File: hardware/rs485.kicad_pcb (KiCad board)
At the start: 2 copper layers, 40 x 40 mm, 43 parts, among them P1 CON-SENSOR, P2 BOOT, P3 CONN_5, SW1 SW_DIP_4, U1 XMC1XXX48, U2 DRILL, U3 DRILL, U4 DRILL, U5 DRILL, U6 SP3491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

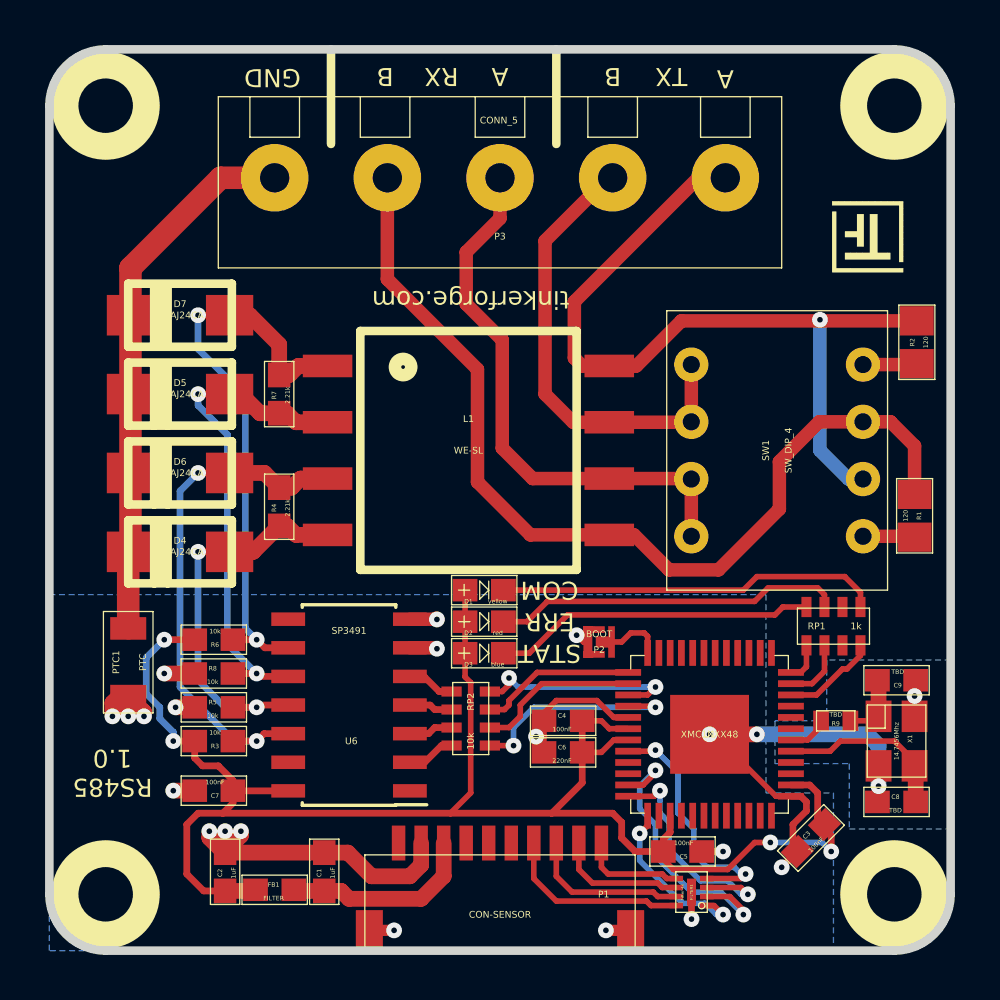
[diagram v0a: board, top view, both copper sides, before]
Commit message: add wee, ce logos, dip description, fiducials
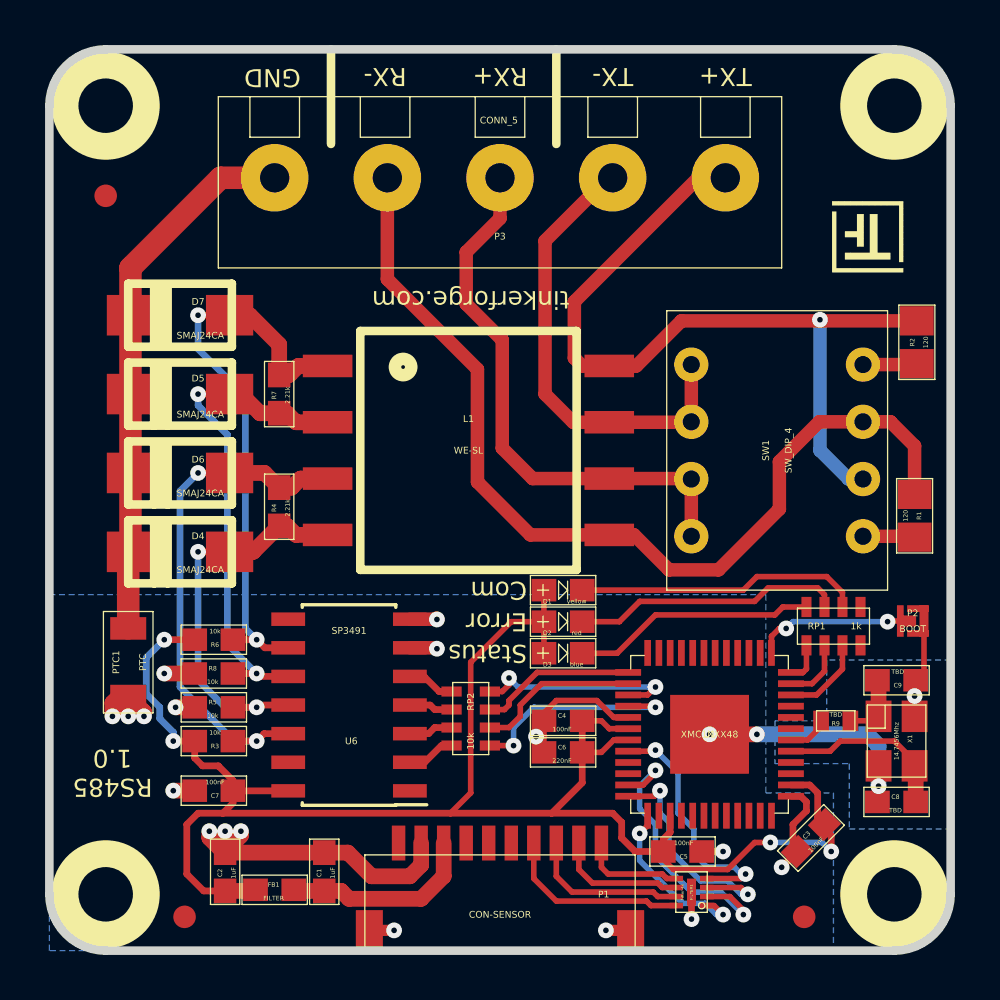
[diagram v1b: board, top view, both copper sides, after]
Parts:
- added Fiducial_Mark: VAL**, kicad-libraries:Fiducial_Mark, F.Cu at (158.8, 121.6)
- added Fiducial_Mark: VAL**, kicad-libraries:Fiducial_Mark, F.Cu at (127.8, 89.6)
- added Fiducial_Mark: VAL**, kicad-libraries:Fiducial_Mark, F.Cu at (131.3, 121.6)
- added VAL: WEEE_7mm_back, kicad-libraries:WEEE_7mm_back, B.Cu at (157.6, 100.1)
- added VAL: CE_5mm, kicad-libraries:CE_5mm, B.Cu at (157.3, 108.1)
- moved P2 13.9 mm to (163.6, 108.5), turned to 180 degrees
- moved D1 3.50 mm to (148.1, 107.1)
- moved D2 3.50 mm to (148.1, 108.5)
- moved D3 3.50 mm to (148.1, 109.9)
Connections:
- RP1 pad 1: Net-(D1-Pad2) -> (no net)
- RP1 pad 2: (no net) -> Net-(D1-Pad2)
- RP1 pad 7: (no net) -> Net-(RP1-Pad7)
- RP1 pad 8: Net-(RP1-Pad8) -> (no net)
- U1 pad 1: (no net) -> Net-(P2-Pad2)
- U1 pad 12: Net-(P2-Pad2) -> (no net)
- U1 pad 46: Net-(RP1-Pad8) -> Net-(RP1-Pad7)
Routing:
- net Net-(D1-Pad2): track 17.0 -> 12.2 mm
- net Net-(RP1-Pad8): track 4.26 -> 0.00 mm
- net Net-(P2-Pad2): track 2.97 -> 7.14 mm, vias 0 -> 2
- net Net-(D2-Pad2): track 15.5 -> 11.5 mm
- net Net-(D3-Pad2): track 14.3 -> 10.3 mm
- net Net-(RP1-Pad7): track 0.00 -> 3.81 mm
- net VCC: track 76.2 -> 79.4 mm
- net GND: track 57.6 -> 55.2 mm, vias 22 -> 21
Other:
- board text added: "1"
- board text added: "2"
- board text added: "3"
- board text added: "4"
- board text added: "Com"
- board text added: "Error"
- board text added: "Full Duplex Non Terminated"
- board text added: "Full Duplex Terminated"
- board text added: "Half Duplex Non Terminated"
- board text added: "Half Duplex Terminated"
- board text added: "ON"
- board text added: "RX+"
- board text added: "RX-"
- board text added: "Status"
- board text added: "TX+"
- board text added: "TX-"
- board text removed: "A"
- board text removed: "B"
- board text removed: "COM"
- board text removed: "ERR"
- board text removed: "RX"
- board text removed: "STAT"
- board text removed: "TX"

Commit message: ordered first prototype
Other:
- board text added: "Full-Duplex Non-Terminated"
- board text added: "Full-Duplex Terminated"
- board text added: "Half-Duplex Non-Terminated"
- board text added: "Half-Duplex Terminated"
- board text removed: "Full Duplex Non Terminated"
- board text removed: "Full Duplex Terminated"
- board text removed: "Half Duplex Non Terminated"
- board text removed: "Half Duplex Terminated"
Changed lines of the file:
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@@
     (visible_elements FFFF7FBF)
     (pcbplotparams
-      (layerselection 0x00030_80000001)
+      (layerselection 0x010f8_80000001)
       (usegerberextensions true)
       (excludeedgelayer true)
@@
     (effects (font (size 0.8 0.8) (thickness 0.15)) (justify mirror))
   )
-  (gr_text "Full Duplex\nTerminated" (at 137.5 112.1 270) (layer B.SilkS)
+  (gr_text "Full-Duplex\nTerminated" (at 137.5 112.1 270) (layer B.SilkS)
     (effects (font (size 0.8 0.8) (thickness 0.15)) (justify mirror))
   )
-  (gr_text "Full Duplex\nNon Terminated" (at 149.55 112.1 270) (layer B.SilkS)
+  (gr_text "Full-Duplex\nNon-Terminated" (at 149.55 112.1 270) (layer B.SilkS)
     (effects (font (size 0.8 0.8) (thickness 0.15)) (justify mirror))
   )
@@
     (effects (font (size 0.8 0.8) (thickness 0.15)) (justify mirror))
   )
-  (gr_text "Half Duplex\nNon Terminated" (at 149.55 100.7 270) (layer B.SilkS)
+  (gr_text "Half-Duplex\nNon-Terminated" (at 149.55 100.7 270) (layer B.SilkS)
     (effects (font (size 0.8 0.8) (thickness 0.15)) (justify mirror))
   )
-  (gr_text "Half Duplex\nTerminated" (at 137.5 100.7 270) (layer B.SilkS)
+  (gr_text "Half-Duplex\nTerminated" (at 137.5 100.7 270) (layer B.SilkS)
     (effects (font (size 0.8 0.8) (thickness 0.15)) (justify mirror))
   )

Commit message: specify crystal and capacitors
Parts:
- C8, C9: value TBD -> 10pF
- X1: value 14.7456Mhz -> 16Mhz
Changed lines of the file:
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@@
     (links 107)
     (no_connects 0)
-    (area 125.109499 82.909499 165.490501 123.290501)
+    (area 124.445139 82.245139 282.895869 162.490743)
     (thickness 1.6002)
     (drawings 125)
@@
   )
   (setup
-    (last_trace_width 0.25)
+    (last_trace_width 0.249)
     (user_trace_width 0.25)
     (user_trace_width 0.29972)
@@
       (effects (font (size 0.2 0.2) (thickness 0.05)))
     )
-    (fp_text value TBD (at 0.05 -0.375 180) (layer F.SilkS)
+    (fp_text value 10pF (at 0.05 -0.375 180) (layer F.SilkS)
       (effects (font (size 0.2 0.2) (thickness 0.05)))
     )
@@
       (effects (font (size 0.2 0.2) (thickness 0.05)))
     )
-    (fp_text value TBD (at 0.05 -0.375) (layer F.SilkS)
+    (fp_text value 10pF (at 0.05 -0.375) (layer F.SilkS)
       (effects (font (size 0.2 0.2) (thickness 0.05)))
     )
@@
       (effects (font (size 0.2 0.2) (thickness 0.05)))
     )
-    (fp_text value 14.7456Mhz (at 0 0 270) (layer F.SilkS)
-      (effects (font (size 0.2 0.2) (thickness 0.05)))
-    )
+    (fp_text value 16Mhz (at 0 0 270) (layer F.SilkS)
+      (effects (font (size 0.2 0.2) (thickness 0.05)))
+    )

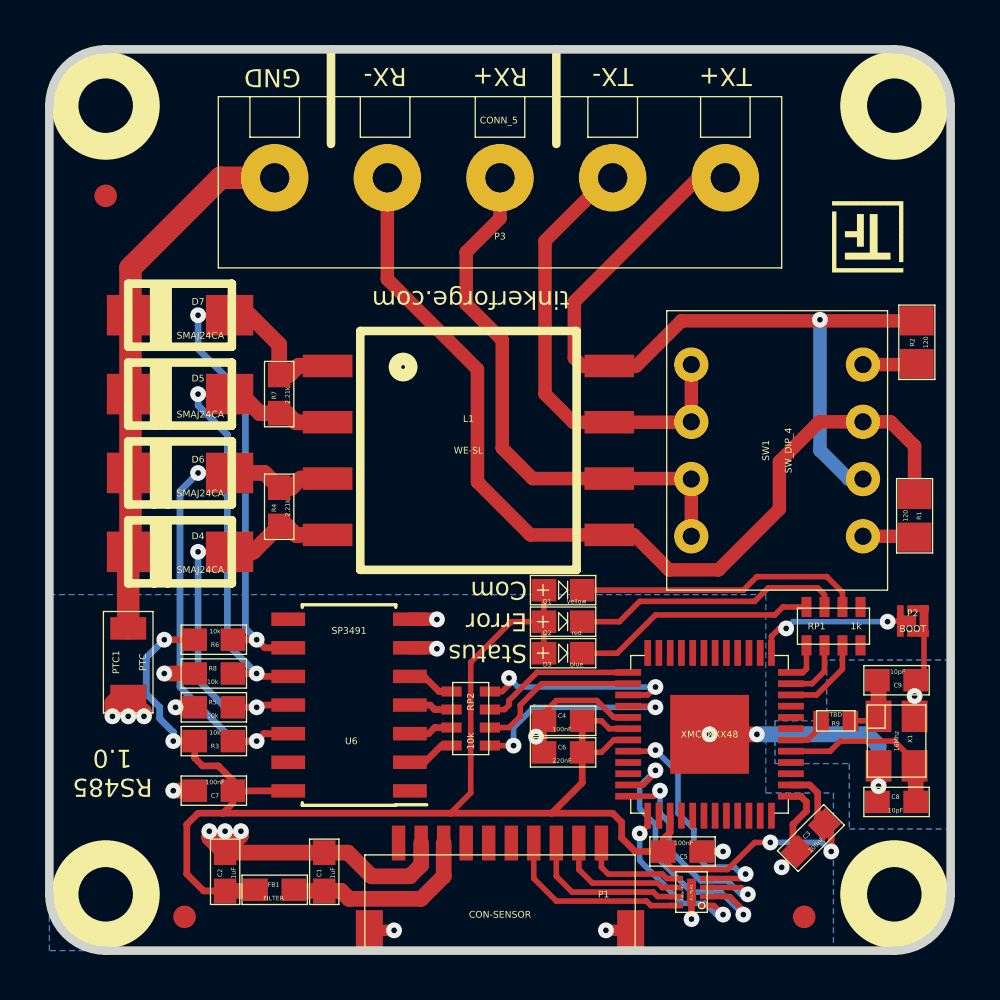
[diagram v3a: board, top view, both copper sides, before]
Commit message: fix footprints
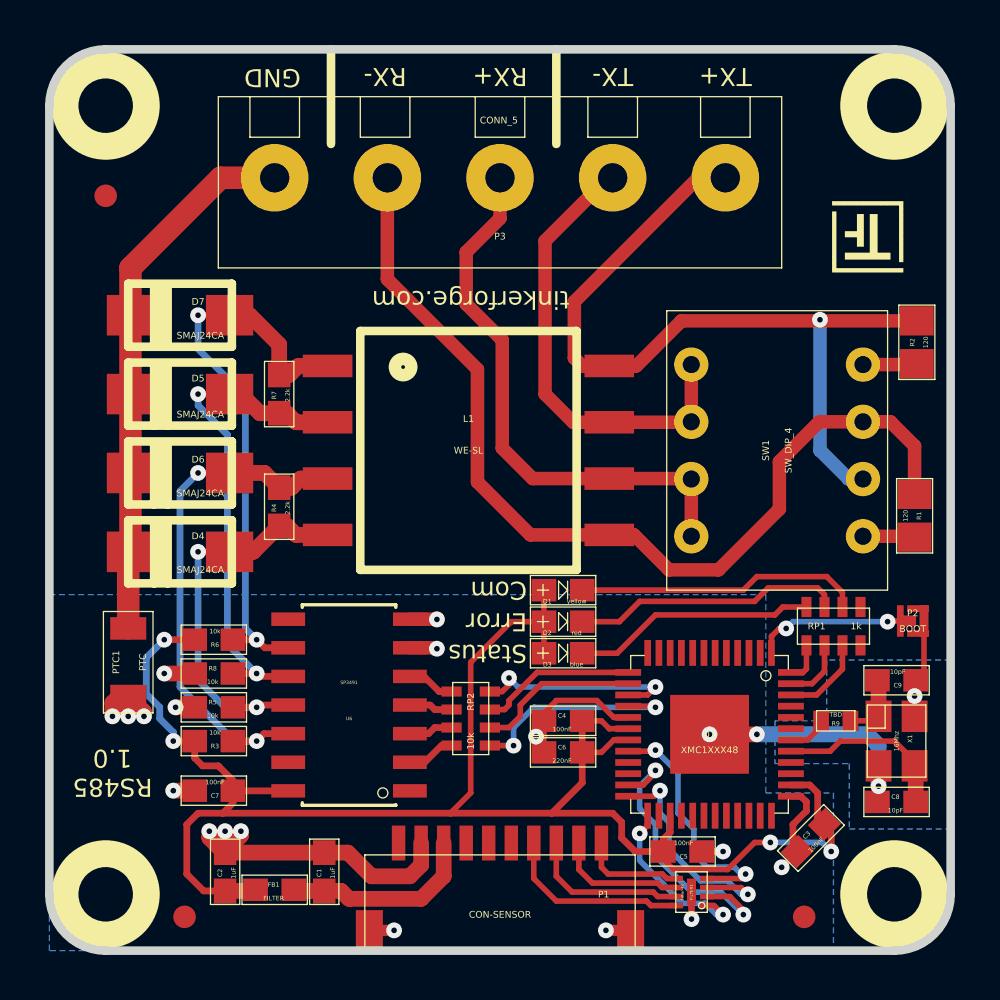
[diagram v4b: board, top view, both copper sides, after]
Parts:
- R4, R7: value 2.21k -> 2.2k
- U6: footprint SOIC-14_3.9x8.7mm_Pitch1.27mm -> kicad-libraries:SOIC-14_3.9x8.7mm_Pitch1.27mm

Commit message: add comcu icon
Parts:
- added G***: LOGO, kicad-libraries:Logo_CoMCU, B.Cu at (157.6, 115.3)
- moved VAL 0.30 mm to (157.6, 108.1)

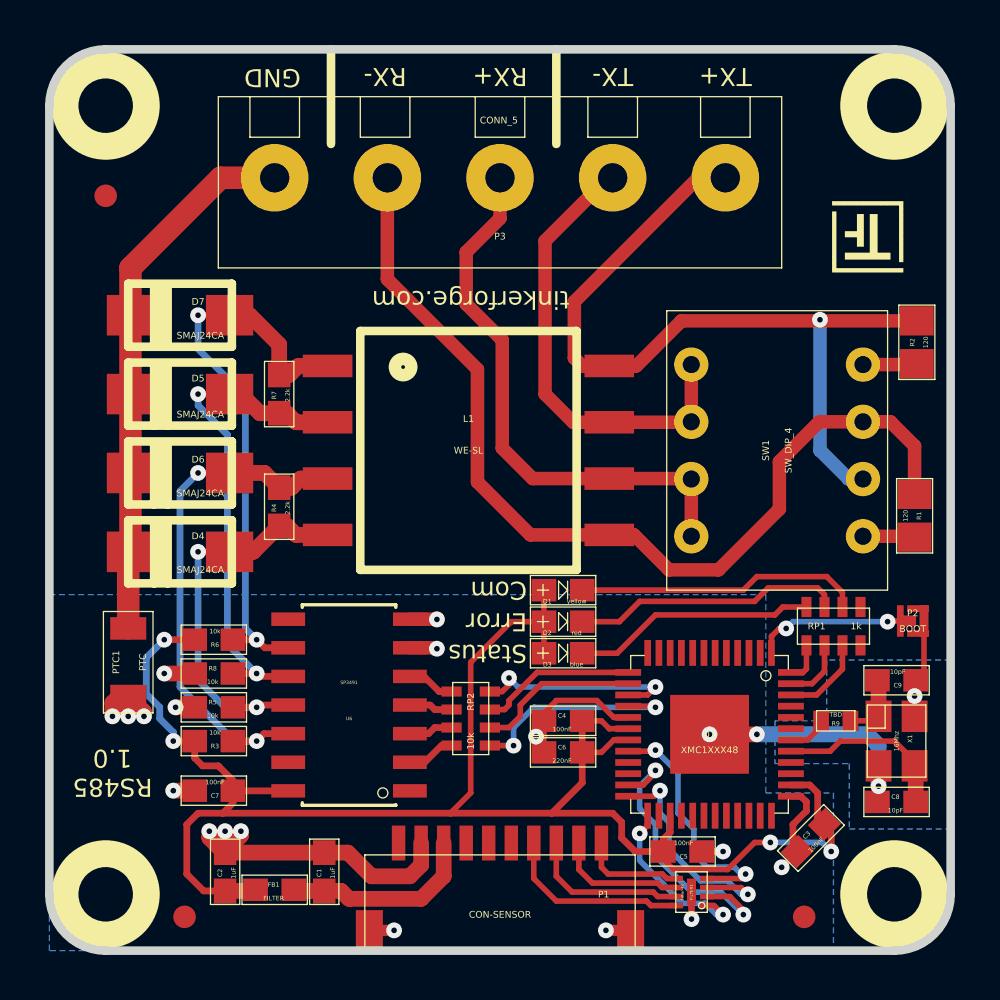
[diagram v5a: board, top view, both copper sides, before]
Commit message: change bricklet connector to 7pole JST GH connector
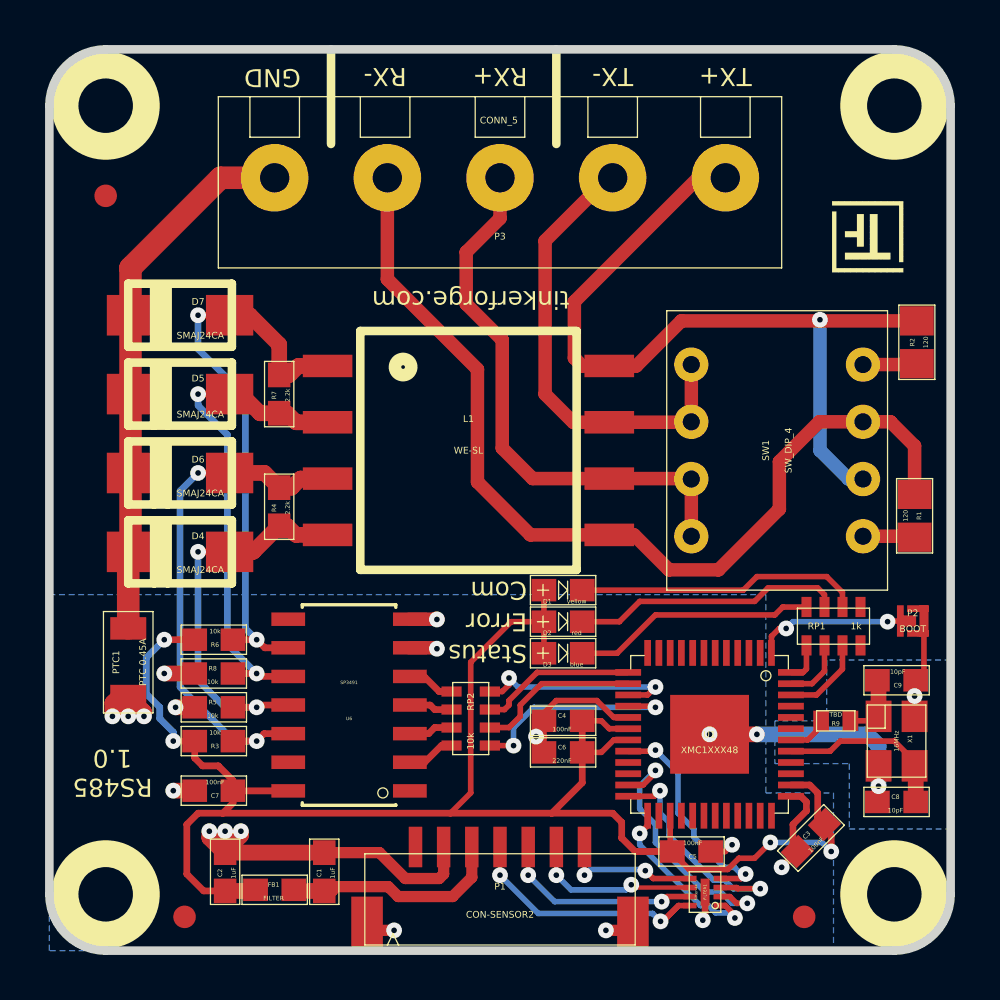
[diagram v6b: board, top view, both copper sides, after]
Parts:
- P1: value CON-SENSOR -> CON-SENSOR2; footprint CON-SENSOR -> kicad-libraries:CON-SENSOR2
- PTC1: value PTC -> PTC 0.45A
- X1: value 16Mhz -> 16MHz
- moved FILTER1 0.60 mm to (154.4, 120.5)
- moved C5 0.40 mm to (153.8, 118.7)
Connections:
- P1 pad 4: (no net) -> Net-(FILTER1-Pad8)
- P1 pad 5: (no net) -> Net-(FILTER1-Pad7)
- P1 pad 6: (no net) -> Net-(FILTER1-Pad6)
- P1 pad 7: Net-(FILTER1-Pad8) -> Net-(FILTER1-Pad5)
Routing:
- net Net-(FILTER1-Pad8): track 8.40 -> 11.9 mm, vias 0 -> 2
- net VCC: track 79.4 -> 81.5 mm
- net Net-(FILTER1-Pad7): track 7.17 -> 9.00 mm, vias 0 -> 2
- net Net-(FILTER1-Pad6): track 5.83 -> 7.59 mm, vias 0 -> 2
- net Net-(FILTER1-Pad5): track 4.61 -> 6.19 mm, vias 0 -> 2
- net GND: track 55.2 -> 56.6 mm
- net Net-(C1-Pad2): track 8.71 -> 9.88 mm
- net S-CLK: track 13.0 -> 11.9 mm
- net S-MISO: track 11.0 -> 10.3 mm
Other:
- net class Default: trace_width 0.249 -> 0.2
- rule trace_min: 0.249 -> 0.2

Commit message: add pulldown resistors for SPI
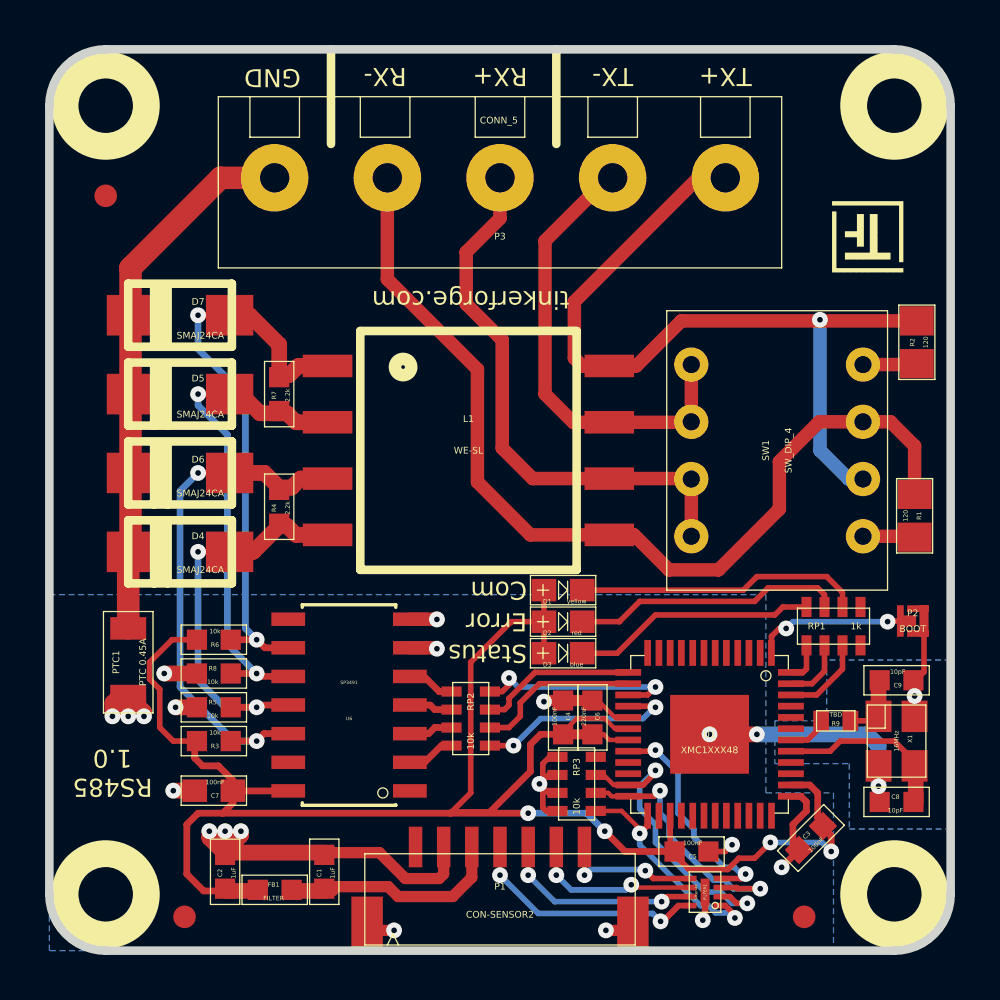
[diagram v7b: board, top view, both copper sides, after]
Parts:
- added RP3: 10k, kicad-libraries:0603X4, F.Cu at (148.7, 115.7)
- C1, C2, C3, C4, C5, C6, C8, C9, FB1, R3, R4, R5, R6, R7, R8: footprint 0603E -> 0603F
- P1: footprint kicad-libraries:CON-SENSOR2 -> CON-SENSOR2
- moved C6 2.02 mm to (149.4, 112.8), turned to 90 degrees
- moved C4 0.15 mm to (148.1, 112.8), turned to 90 degrees
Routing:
- net GND: track 56.6 -> 59.8 mm, vias 21 -> 22
- net S-CS: track 7.96 -> 10.4 mm
- net VCC: track 81.5 -> 83.8 mm
- net S-CLK: track 11.9 -> 13.5 mm
- net S-MOSI: track 10.5 -> 12.0 mm
